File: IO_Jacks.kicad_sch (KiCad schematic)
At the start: 53 parts

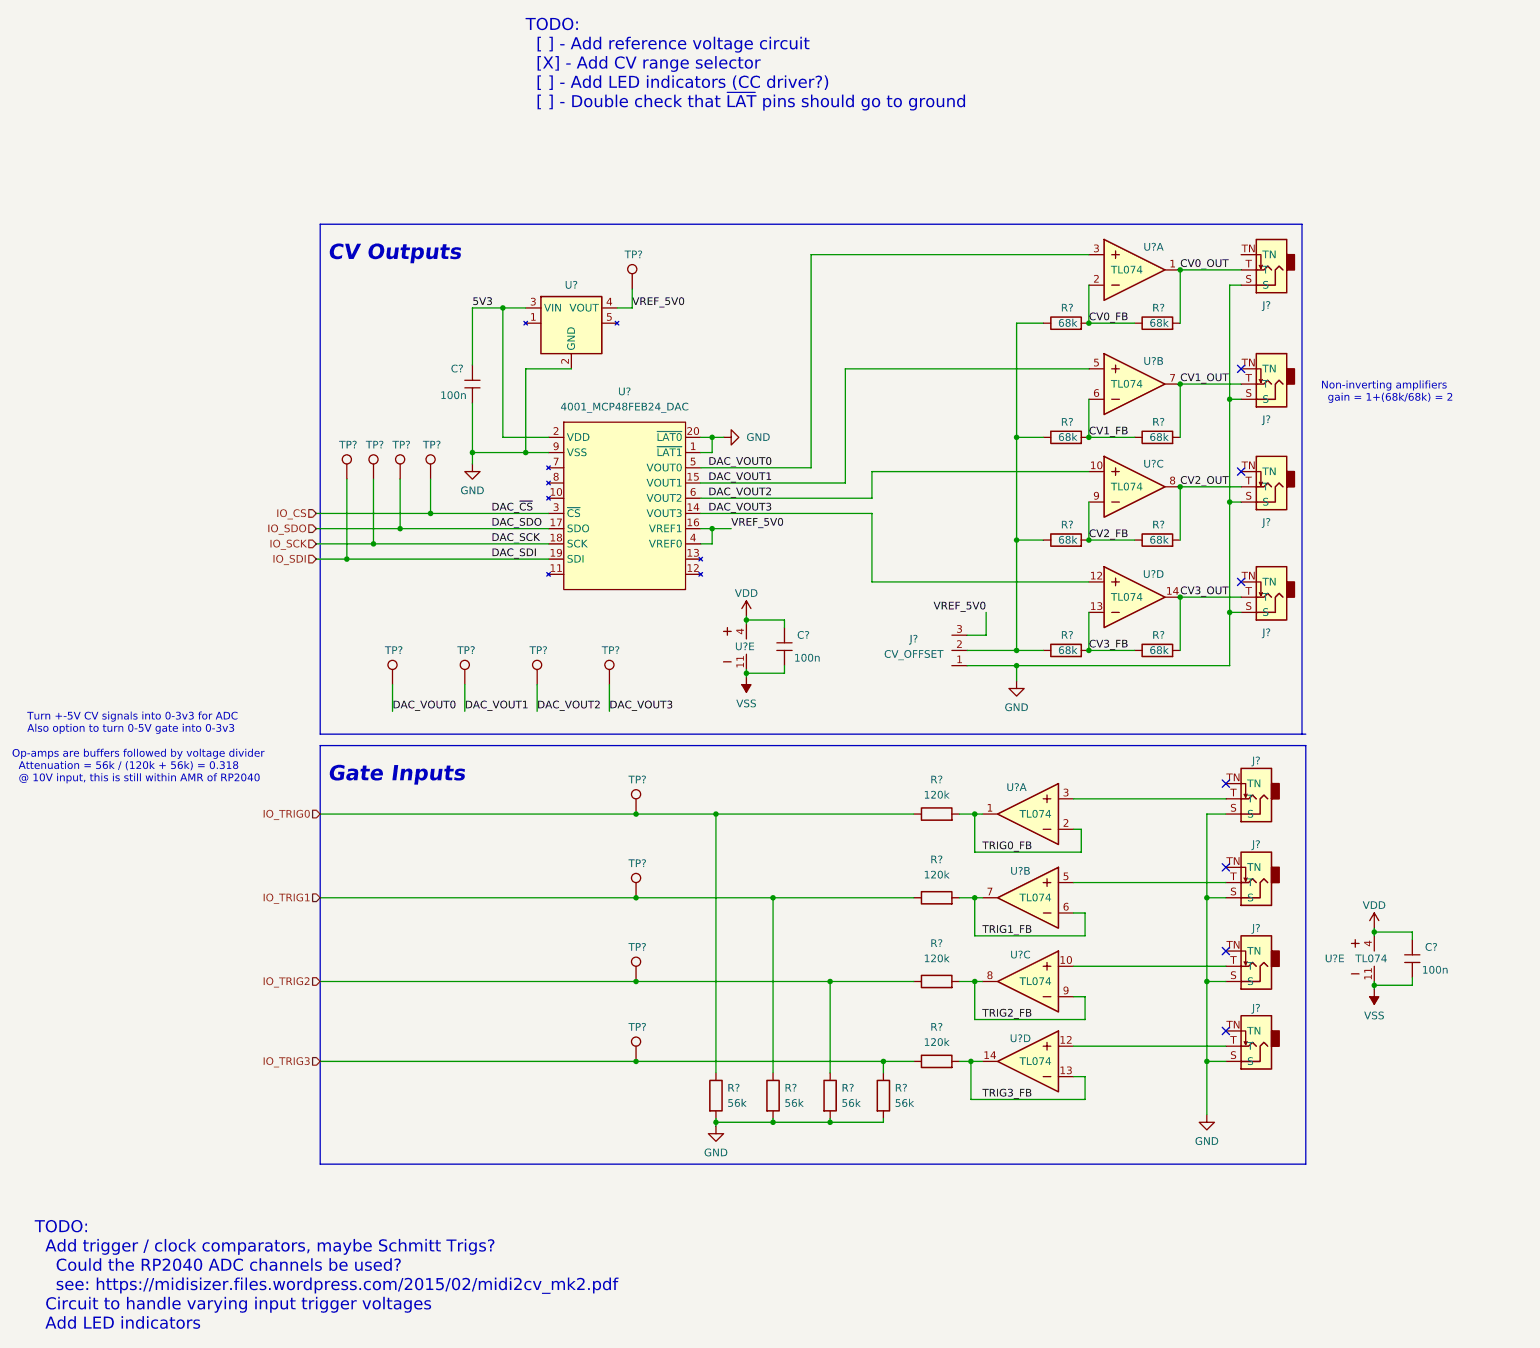
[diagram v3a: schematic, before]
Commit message: ran ERC, minimal errors. Imported footprints and started grouping them
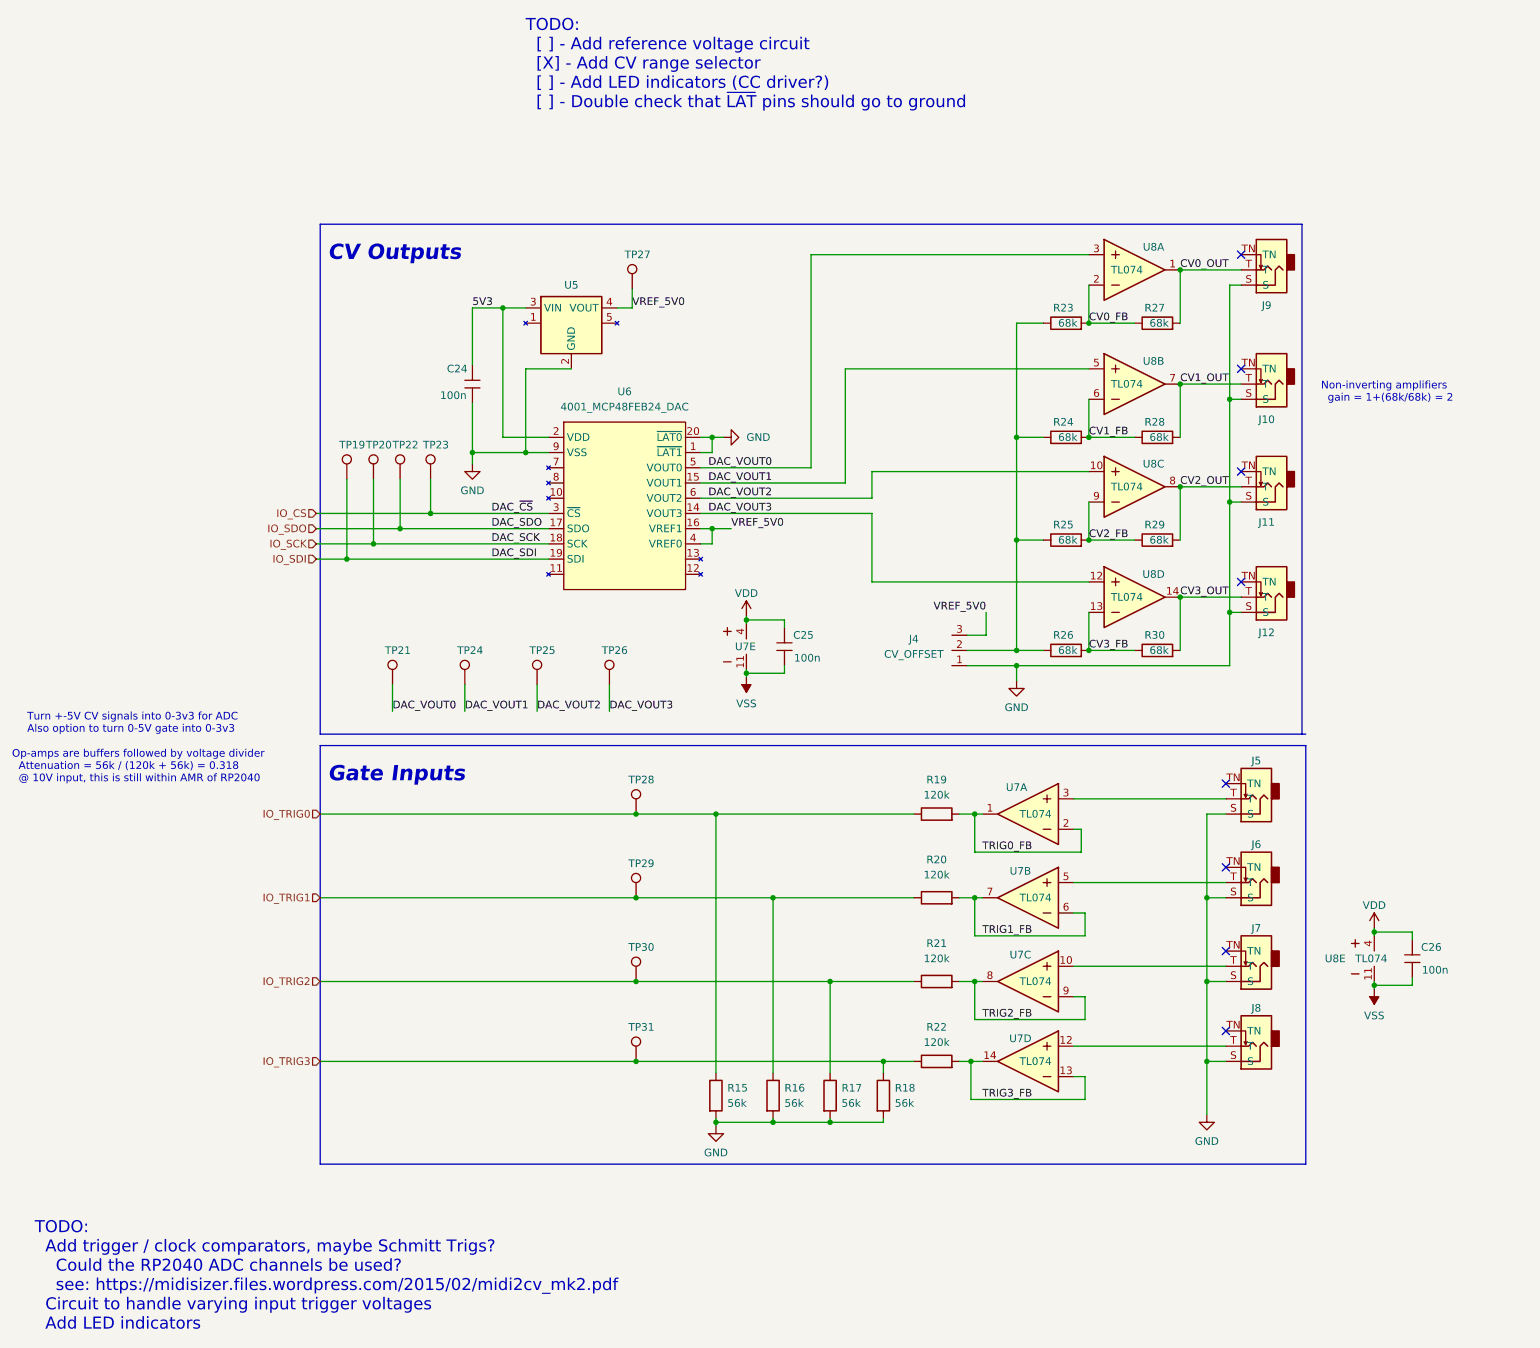
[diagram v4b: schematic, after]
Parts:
- R15, R16, R17, R18, R19, R20, R21, R22, R23, R24, R25, R26, R27, R28, R29, R30: renamed from R?; footprint Shulltronics_Passives:Resistor_0402 -> Shulltronics_Generics:RES-0402
- gave numbers to parts that had none: 29
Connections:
- no-connect marks 7 -> 8

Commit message: more work on pcb, added some TODO notes to schematic
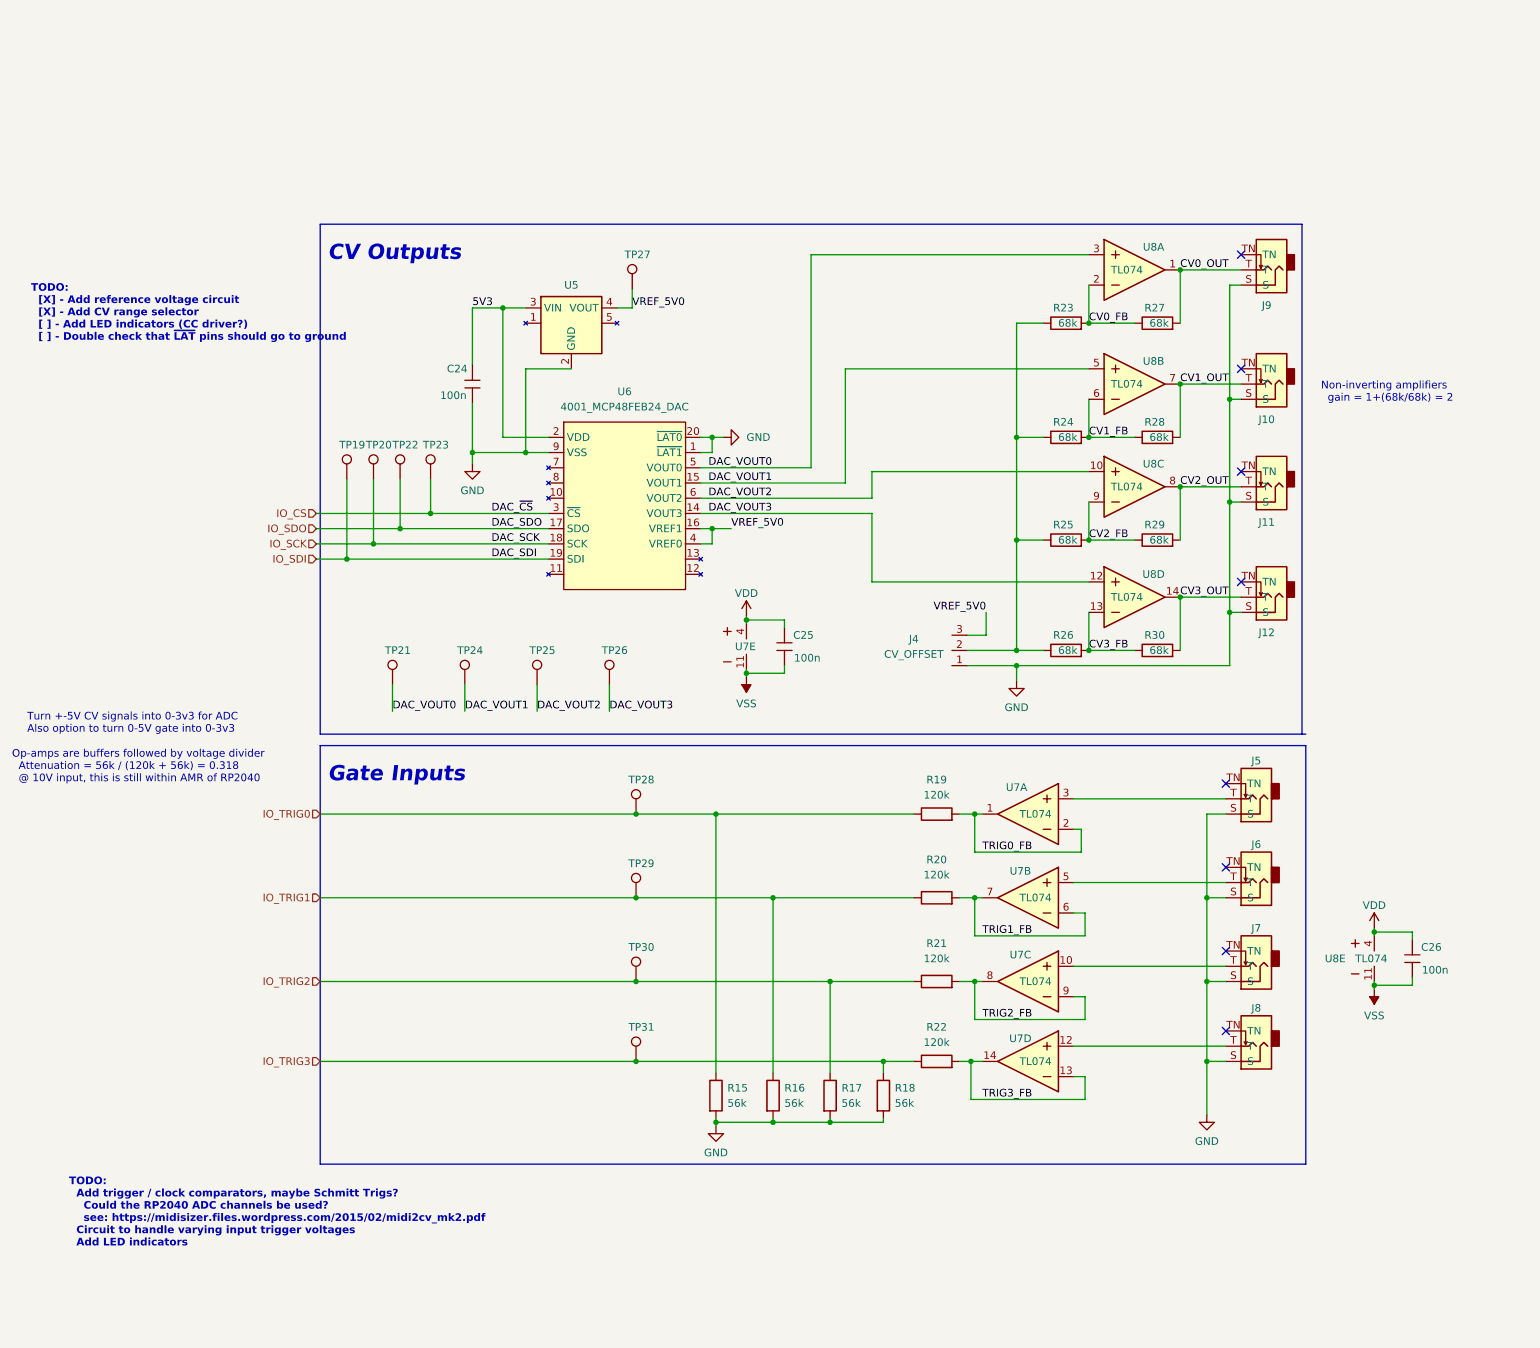
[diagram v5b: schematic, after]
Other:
- note added: "TODO: [X] - Add reference voltage circuit [X] - Add CV range selector [ ] - Add LED indicators (CC driver?) [ ] - Double check that ~{LAT} pins should go to ground"
- note removed: "TODO: [ ] - Add reference voltage circuit [X] - Add CV range selector [ ] - Add LED indicators (CC driver?) [ ] - Double check that ~{LAT} pins should go to ground"
- company: (none) -> Shulltronics
- title: (none) -> Binary CV Sequencer
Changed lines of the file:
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@@
 (kicad_sch (version 20211123) (generator eeschema)
   (paper "USLetter")
+  (title_block
+    (title "Binary CV Sequencer")
+    (date "2022-03-11")
+    (rev "0.1")
+    (company "Shulltronics")
+  )
   (junction (at 140.335 163.83) (diameter 0) (color 0 0 0 0)
   )
@@
     (stroke (width 0) (type default) (color 0 0 0 0))
   )
-  (text "TODO:\n  [ ] - Add reference voltage circuit\n  [X] - Add CV range selector\n  [ ] - Add LED indicators (CC driver?)\n  [ ] - Double check that ~{LAT} pins should go to ground\n"
-    (at 99.06 -5.08 0)
-    (effects (font (size 2 2)) (justify left bottom))
+  (text "TODO:\n  [X] - Add reference voltage circuit\n  [X] - Add CV range selector\n  [ ] - Add LED indicators (CC driver?)\n  [ ] - Double check that ~{LAT} pins should go to ground\n"
+    (at 16.51 33.655 0)
+    (effects (font (size 1.27 1.27) (thickness 0.254) bold) (justify left bottom))
   )
   (text "Gate Inputs" (at 66.04 107.315 0)
@@
   )
   (text "TODO:\n  Add trigger / clock comparators, maybe Schmitt Trigs?\n    Could the RP2040 ADC channels be used?\n    see: https://midisizer.files.wordpress.com/2015/02/midi2cv_mk2.pdf\n  Circuit to handle varying input trigger voltages\n  Add LED indicators\n"
-    (at 17.145 198.755 0)
-    (effects (font (size 2 2)) (justify left bottom))
+    (at 22.86 184.785 0)
+    (effects (font (size 1.27 1.27) (thickness 0.254) bold) (justify left bottom))
   )
   (text "Non-inverting amplifiers\n  gain = 1+(68k/68k) = 2" (at 231.775 43.815 0)

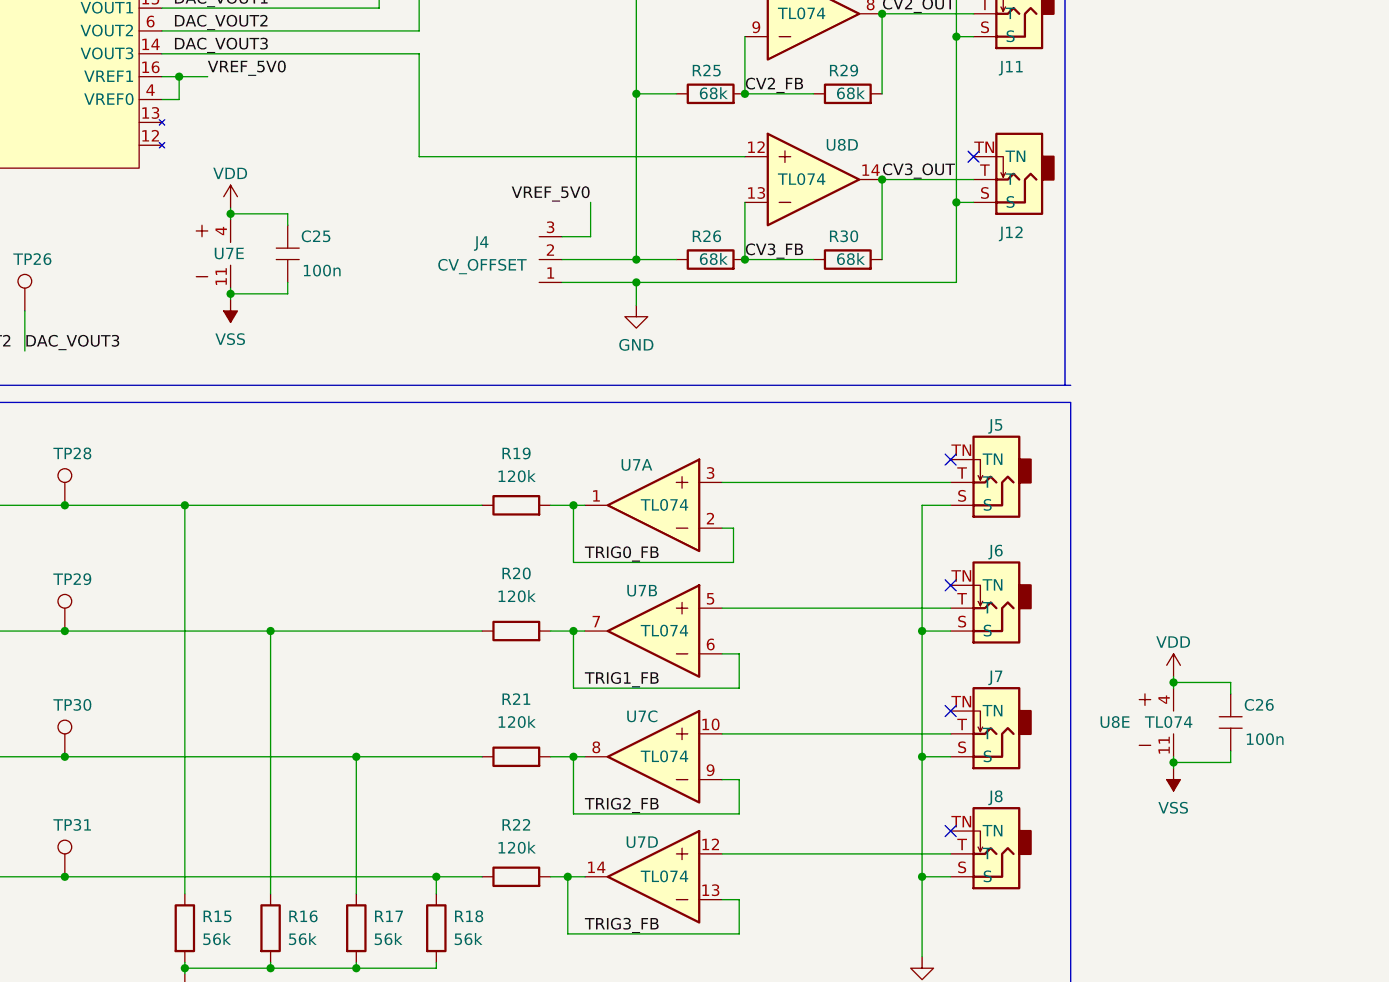
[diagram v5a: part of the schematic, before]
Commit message: Changed encoder to SMD version
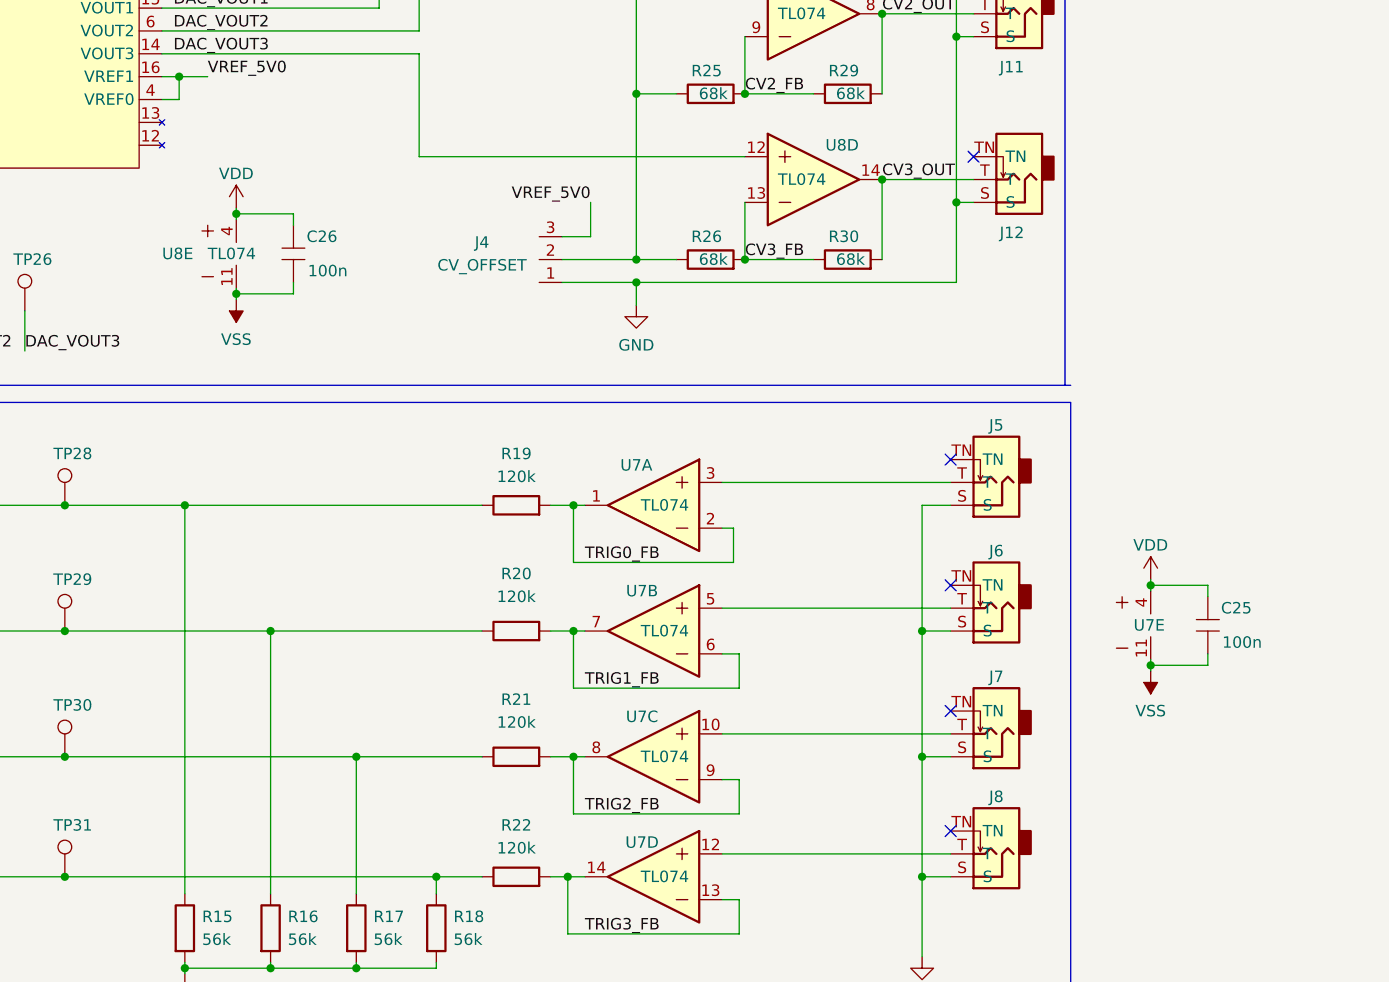
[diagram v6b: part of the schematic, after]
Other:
- moved on the sheet: C25, C26, U7E, U8E
